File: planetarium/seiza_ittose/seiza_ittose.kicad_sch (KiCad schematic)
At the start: 28 parts, among them J1 Jack-DC, J10 Jack-DC, J11 Jack-DC, J12 Jack-DC, J13 Jack-DC, J2 Jack-DC, J3 Jack-DC, J4 Jack-DC, J5 Jack-DC, J6 Jack-DC, J7 Jack-DC, J8 Jack-DC, J9 Jack-DC, Q1 NP52N06SLG, Q2 NP52N06SLG, Q3 NP52N06SLG, Q4 NP52N06SLG, Q5 NP52N06SLG, Q6 NP52N06SLG, Q7 NP52N06SLG, Q8 NP52N06SLG, Q9 NP52N06SLG, U1 XIAO-ESP32-C3-SMD

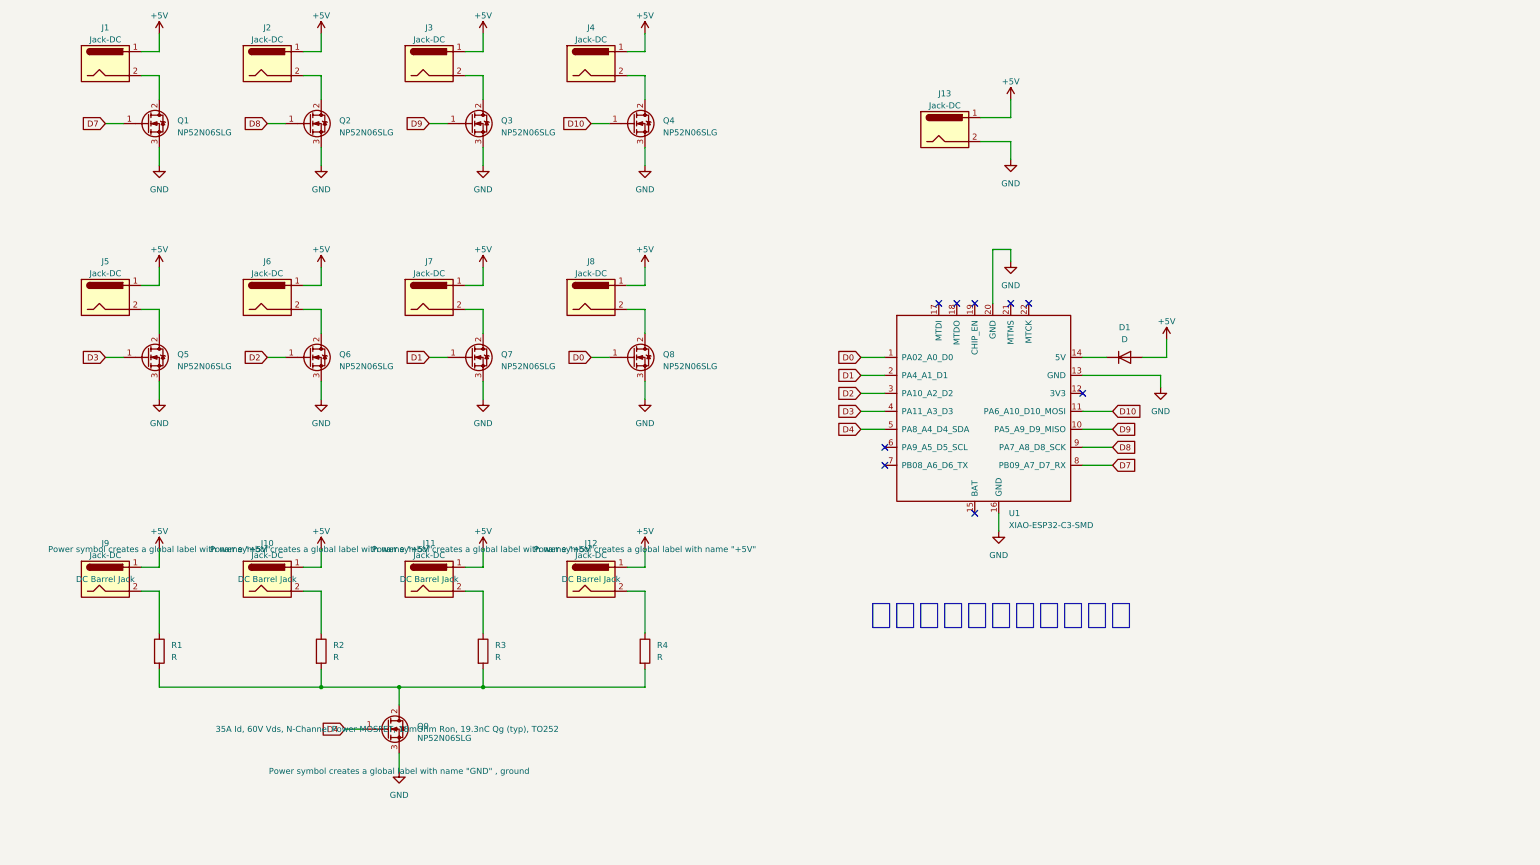
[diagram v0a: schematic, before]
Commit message: add: 恒星、一等星、星座基板を新調
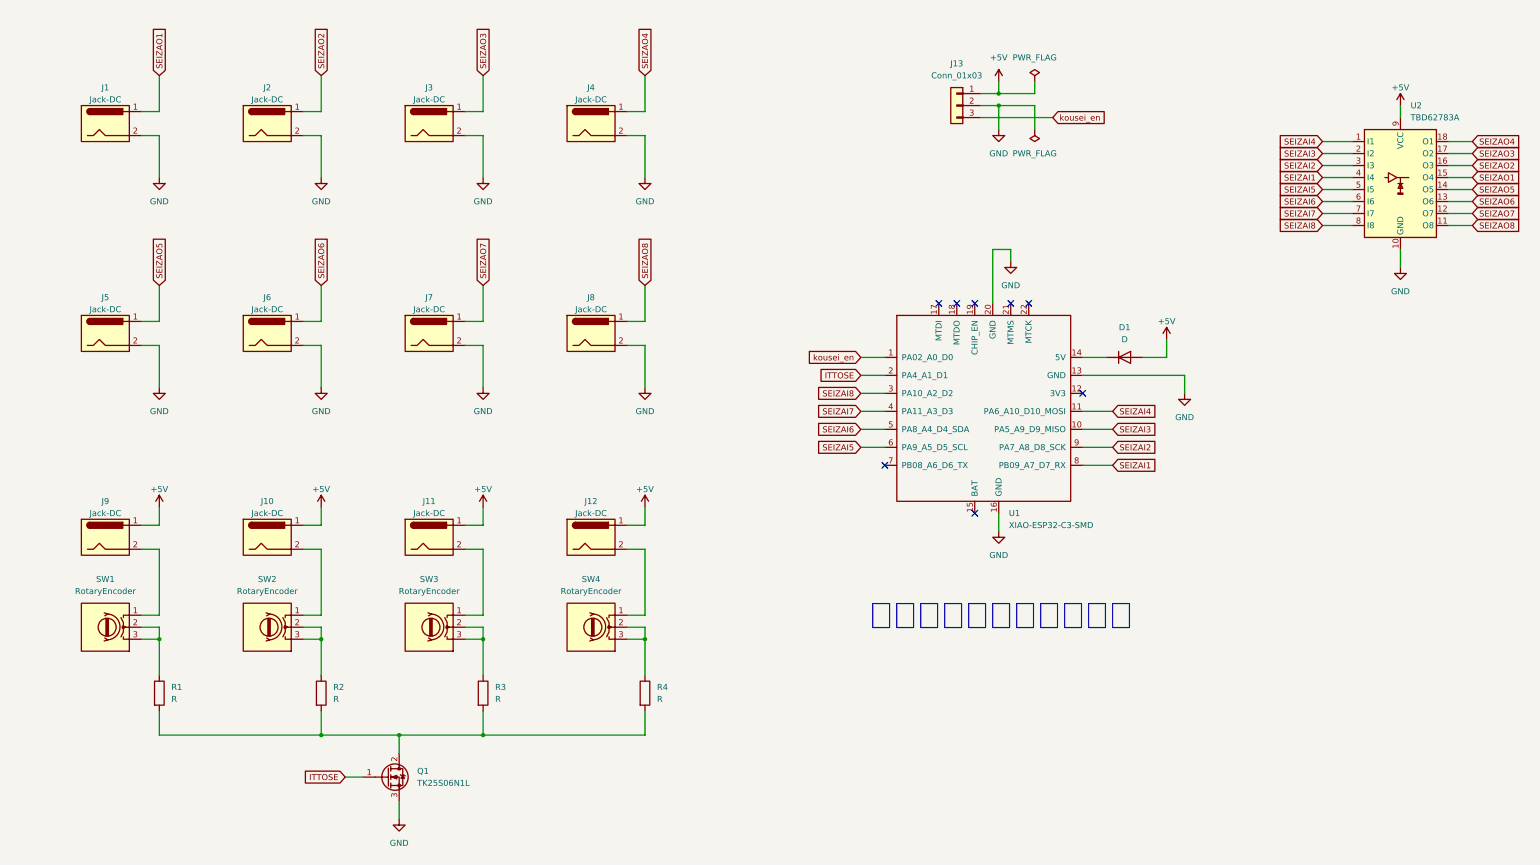
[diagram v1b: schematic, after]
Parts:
- removed J13: Jack-DC, DCJack:DCJack, symbol Connector:Jack-DC
- removed Q2, Q3, Q4, Q5, Q6, Q7, Q8, Q9: NP52N06SLG, Package_TO_SOT_SMD:TO-252-2, symbol Transistor_FET:QM6006D
- added J13: Conn_01x03, Connector_PinHeader_2.54mm:PinHeader_1x03_P2.54mm_Vertical, symbol Connector_Generic:Conn_01x03
- added SW1, SW2, SW3, SW4: RotaryEncoder, VR:VR, symbol Device:RotaryEncoder
- added U2: TBD62783A, Package_SO:SOP-18_7x12.5mm_P1.27mm, symbol Transistor_Array:TBD62783A
- Q1: value NP52N06SLG -> TK25S06N1L
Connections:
- net +5V: now also J13.1 (Pin_1), U2.9 (VCC); no longer J1.1, J2.1, J3.1, J4.1, J5.1, J6.1, J7.1, J8.1
- net GND: now also J1.2, J2.2, J3.2, J4.2, J5.2, J6.2, J7.2, J8.2, J13.2 (Pin_2), U2.10 (GND)
- net at J11.2: now also SW3.1; no longer R3.1
- net at R1.2, R2.2, R3.2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: now also Q1.2 (D)
- net SEIZAI5: now reaches U1.6 (PA9_A5_D5_SCL)
- net SEIZAI5: now also U2.5 (I5)
- net at R2.1: now also SW2.2, SW2.3; no longer J10.2
- net at R1.1: now also SW1.2, SW1.3; no longer J9.2
- net at J12.2: now also SW4.1; no longer R4.1
- net D0 renamed kousei_en
- net kousei_en: now also J13.3 (Pin_3)
- net D1 renamed ITTOSE
- net ITTOSE: now also Q1.1 (G)
- net D10 renamed SEIZAI4
- net SEIZAI4: now also U2.1 (I1)
- net D2 renamed SEIZAI8
- net SEIZAI8: now also U2.8 (I8)
- net D3 renamed SEIZAI7
- net SEIZAI7: now also U2.7 (I7)
- net D4 renamed SEIZAI6
- net SEIZAI6: now also U2.6 (I6)
- net D7 renamed SEIZAI1
- net SEIZAI1: now also U2.4 (I4); no longer Q1.1 (G)
- net D8 renamed SEIZAI2
- net SEIZAI2: now also U2.3 (I3)
- net D9 renamed SEIZAI3
- net SEIZAI3: now also U2.2 (I2)
- new net: R3.1, SW3.2, SW3.3
- new net: R4.1, SW4.2, SW4.3
- new net: J10.2, SW2.1
- new net: J9.2, SW1.1
- new net SEIZAO1: J1.1, U2.15 (O4)
- new net SEIZAO2: J2.1, U2.16 (O3)
- new net SEIZAO3: J3.1, U2.17 (O2)
- new net SEIZAO4: J4.1, U2.18 (O1)
- new net SEIZAO5: J5.1, U2.14 (O5)
- new net SEIZAO6: J6.1, U2.13 (O6)
- new net SEIZAO7: J7.1, U2.12 (O7)
- new net SEIZAO8: J8.1, U2.11 (O8)
- no-connect marks 9 -> 8
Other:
- moved on the sheet: J1, J10, J11, J12, J2, J3, J4, J5, J6, J7, J8, J9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

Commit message: change: LED追加, EN->nEN
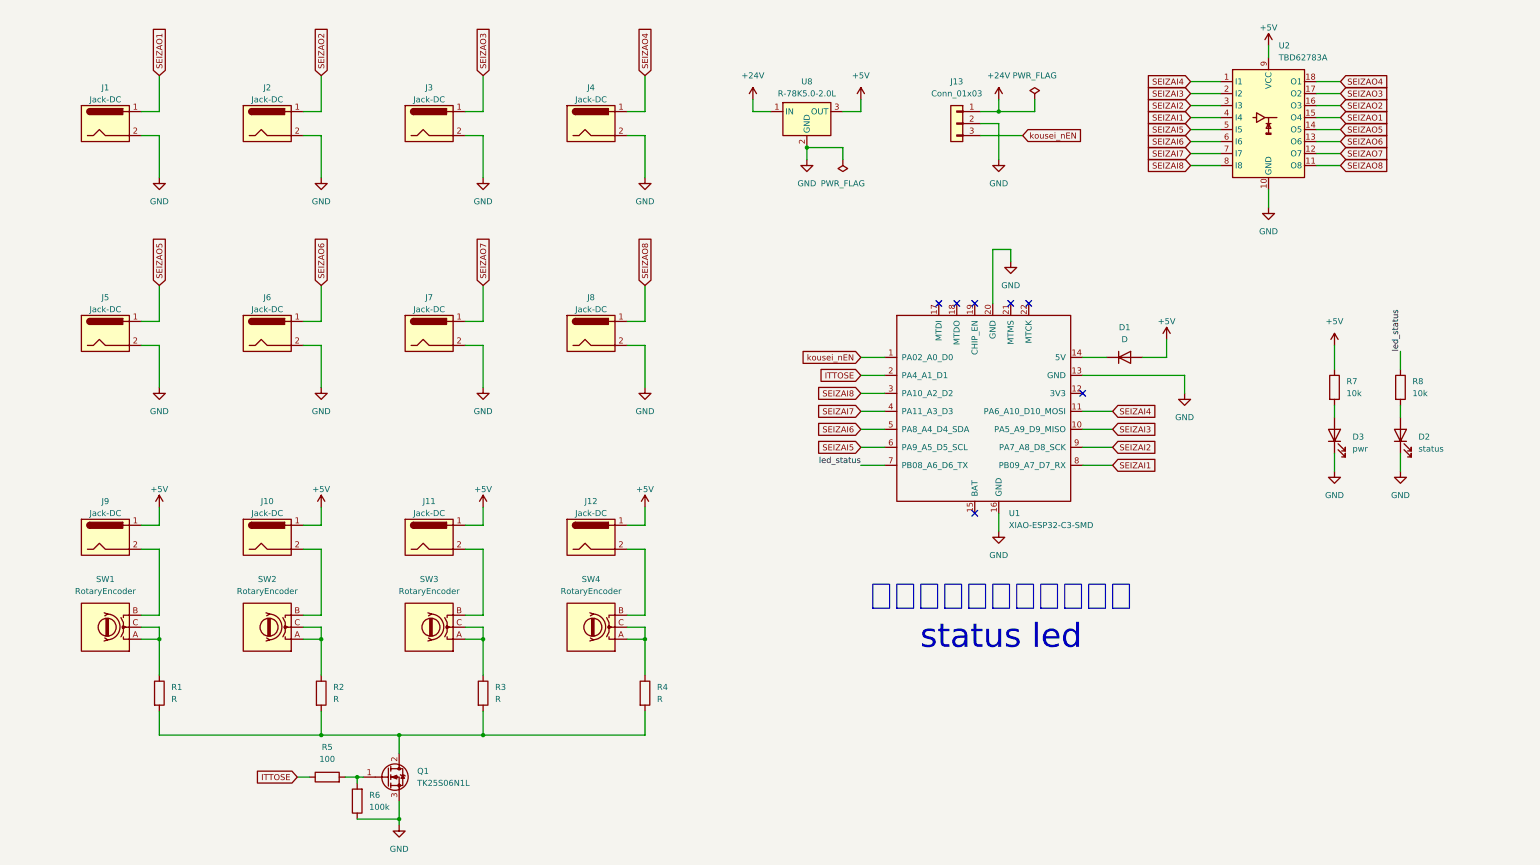
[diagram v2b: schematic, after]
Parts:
- added D2: status, LED_SMD:LED_0603_1608Metric, symbol Device:LED
- added D3: pwr, LED_SMD:LED_0603_1608Metric, symbol Device:LED
- added R5: 100, Resistor_SMD:R_0402_1005Metric, symbol Device:R
- added R6: 100k, Resistor_SMD:R_0402_1005Metric, symbol Device:R
- added R7, R8: 10k, Resistor_SMD:R_0402_1005Metric_Pad0.72x0.64mm_HandSolder, symbol Device:R
- added U8: R-78K5.0-2.0L, R-78K5.0-2.0L:R-78K5.0-2.0L, symbol Converter_DCDC:OKI-78SR-3.3_1.5-W36H-C
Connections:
- net +5V: now also R7.1, U8.3 (OUT); no longer J13.1 (Pin_1)
- net GND: now also D2.1 (K), D3.1 (K), R6.1, U8.2 (GND)
- net ITTOSE: now also R5.1; no longer Q1.1 (G)
- net at J11.2: now also SW3.B; no longer SW3.1
- net led_status: now reaches U1.7 (PB08_A6_D6_TX)
- net led_status: now also R8.1
- net at J12.2: now also SW4.B; no longer SW4.1
- net at J10.2: now also SW2.B; no longer SW2.1
- net at J9.2: now also SW1.B; no longer SW1.1
- net kousei_en renamed kousei_nEN
- new net: R3.1, SW3.A, SW3.C
- new net: Q1.1 (G), R5.2, R6.2
- new net: D2.2 (A), R8.2
- new net: R2.1, SW2.A, SW2.C
- new net: R1.1, SW1.A, SW1.C
- new net: R4.1, SW4.A, SW4.C
- new net: D3.2 (A), R7.2
- new net +24V: J13.1 (Pin_1), U8.1 (IN)
- no-connect marks 8 -> 7
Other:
- note added: "要検討 アンテナの位置 status led"
- note removed: "要検討 アンテナの位置"
- moved on the sheet: J13, U2
